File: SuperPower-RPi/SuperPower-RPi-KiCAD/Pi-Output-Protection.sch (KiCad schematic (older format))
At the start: 5 parts, among them U6 NCP380LMUAJAATBG

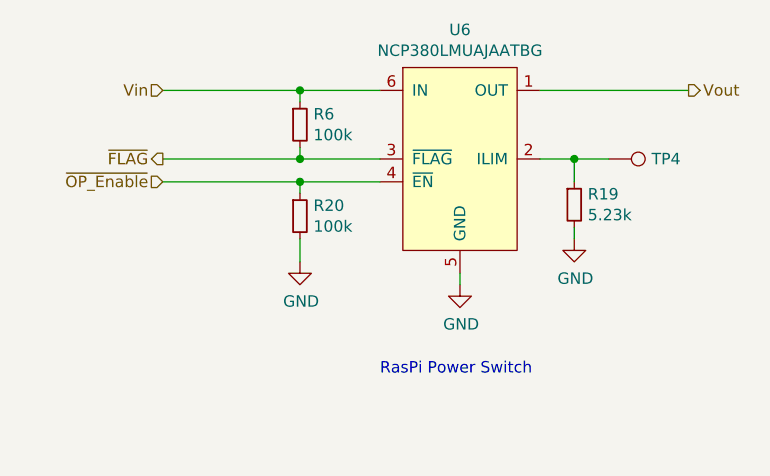
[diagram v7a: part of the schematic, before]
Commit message: Changed Current Limit chip to Enable High, and changed the pull-up to connect to 3.3V
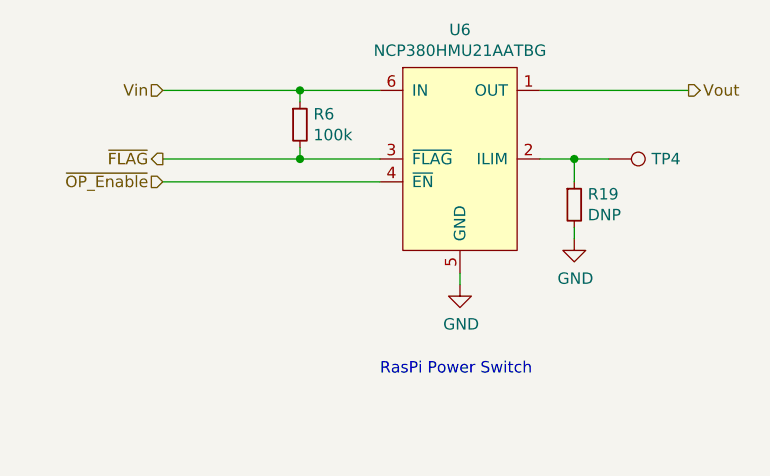
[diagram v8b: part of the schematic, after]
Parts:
- removed R20: 100k, Resistor_SMD:R_0402_1005Metric, symbol Device:R_Small
- R19: value 5.23k -> DNP; Digi-Key PN 311-5.23KHRCT-ND -> DNP; Mfg Yageo -> DNP; Mfg PN RC0603FR-075K23L -> DNP
- U6: value NCP380LMUAJAATBG -> NCP380HMU21AATBG; Digi-Key PN NCP380LMUAJAATBGOSCT-ND -> NCP380HMU21AATBGOSCT-ND; Mfg PN NCP380LMUAJAATBG -> NCP380HMU21AATBG
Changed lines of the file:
@@
 P 6000 3950
 F 0 "R19" H 6059 3996 50  0000 L CNN
-F 1 "5.23k" H 6059 3905 50  0000 L CNN
+F 1 "DNP" H 6059 3905 50  0000 L CNN
 F 2 "Resistor_SMD:R_0603_1608Metric" H 6000 3950 50  0001 C CNN
 F 3 "~" H 6000 3950 50  0001 C CNN
-F 4 "311-5.23KHRCT-ND" H 6000 3950 50  0001 C CNN "Digi-Key PN"
-F 5 "Yageo" H 6000 3950 50  0001 C CNN "Mfg"
-F 6 "RC0603FR-075K23L" H 6000 3950 50  0001 C CNN "Mfg PN"
+F 4 "DNP" H 6000 3950 50  0001 C CNN "Digi-Key PN"
+F 5 "DNP" H 6000 3950 50  0001 C CNN "Mfg"
+F 6 "DNP" H 6000 3950 50  0001 C CNN "Mfg PN"
 	1    6000 3950
 	1    0    0    -1
@@
 	6000 4100 6000 4050
 Wire Wire Line
-	4200 3850 4800 3850
-Wire Wire Line
 	4800 3750 4200 3750
 Connection ~ 4800 3750
@@
 P 5500 3650
 F 0 "U6" H 5500 4115 50  0000 C CNN
-F 1 "NCP380LMUAJAATBG" H 5500 4024 50  0000 C CNN
+F 1 "NCP380HMU21AATBG" H 5500 4024 50  0000 C CNN
 F 2 "SuperPower-RPi-KiCAD:UDFN-6-1EP_2x2mm_P0.65mm_EP0.95x1.7mm" H 5550 3800 50  0001 C CNN
 F 3 "https://www.onsemi.com/pub/Collateral/NCP380-D.PDF" H 5550 3800 50  0001 C CNN
 F 4 "On Semi" H 5500 3650 50  0001 C CNN "Mfg"
-F 5 "NCP380LMUAJAATBG" H 5500 3650 50  0001 C CNN "Mfg PN"
-F 6 "NCP380LMUAJAATBGOSCT-ND" H 5500 3650 50  0001 C CNN "Digi-Key PN"
+F 5 "NCP380HMU21AATBG" H 5500 3650 50  0001 C CNN "Mfg PN"
+F 6 "NCP380HMU21AATBGOSCT-ND" H 5500 3650 50  0001 C CNN "Digi-Key PN"
 	1    5500 3650
 	1    0    0    -1
@@
 Wire Wire Line
 	5850 3450 6500 3450
-$Comp
-L Device:R_Small R20
-U 1 1 5FE4EBC2
-P 4800 4000
-F 0 "R20" H 4859 4046 50  0000 L CNN
-F 1 "100k" H 4859 3955 50  0000 L CNN
-F 2 "Resistor_SMD:R_0402_1005Metric" H 4800 4000 50  0001 C CNN
-F 3 "~" H 4800 4000 50  0001 C CNN
-F 4 "311-100KLRCT-ND" H 4800 4000 50  0001 C CNN "Digi-Key PN"
-F 5 "Yageo" H 4800 4000 50  0001 C CNN "Mfg"
-F 6 "RC0402FR-07100KL" H 4800 4000 50  0001 C CNN "Mfg PN"
-	1    4800 4000
-	1    0    0    -1
-$EndComp
-Wire Wire Line
-	4800 3900 4800 3850
-Connection ~ 4800 3850
-Wire Wire Line
-	4800 3850 5150 3850
-$Comp
-L power:GND #PWR051
-U 1 1 5FE4EF9E
-P 4800 4200
-F 0 "#PWR051" H 4800 3950 50  0001 C CNN
-F 1 "GND" H 4805 4027 50  0000 C CNN
-F 2 "" H 4800 4200 50  0001 C CNN
-F 3 "" H 4800 4200 50  0001 C CNN
-	1    4800 4200
-	1    0    0    -1
-$EndComp
-Wire Wire Line
-	4800 4200 4800 4100
 $Comp
 L Connector:TestPoint TP?
@@
 	6150 3750 6000 3750
 Connection ~ 6000 3750
+Wire Wire Line
+	4200 3850 5150 3850
 $EndSCHEMATC
